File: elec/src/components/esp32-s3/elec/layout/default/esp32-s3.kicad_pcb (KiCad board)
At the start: 2 copper layers, 6 parts

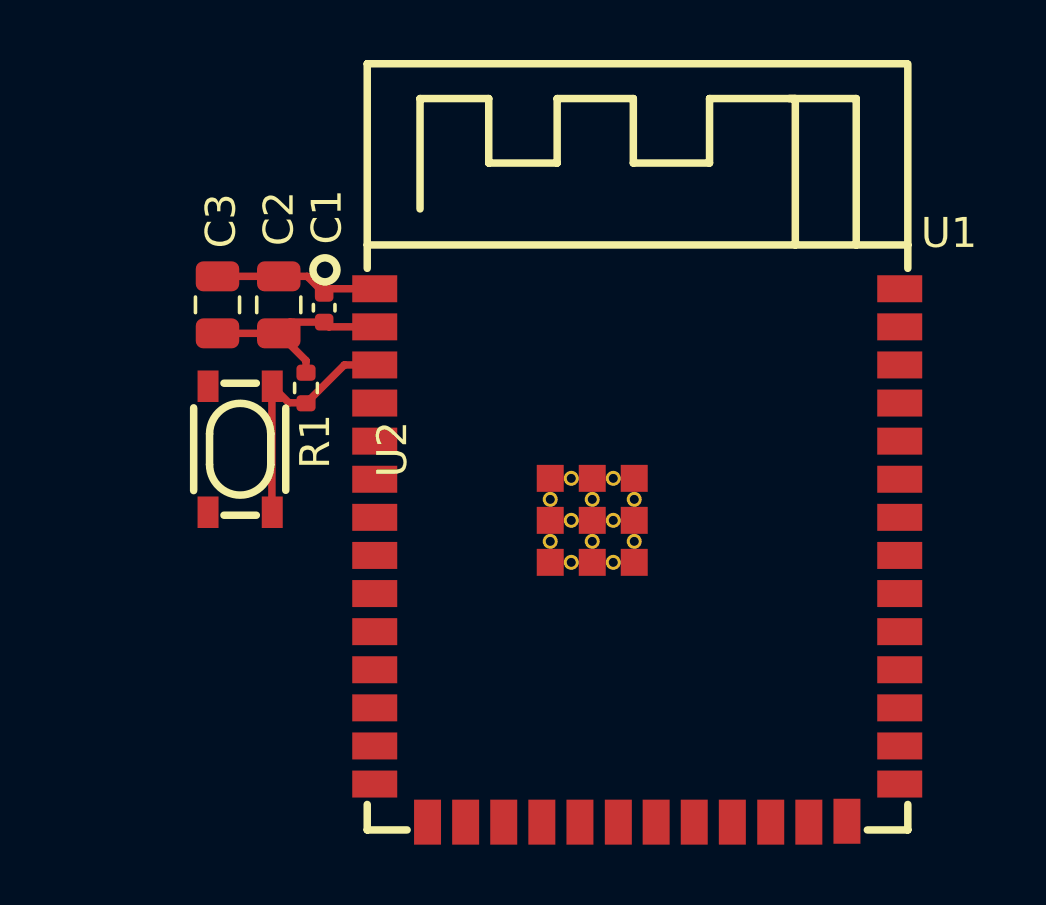
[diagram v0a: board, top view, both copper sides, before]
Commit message: Layout controller block
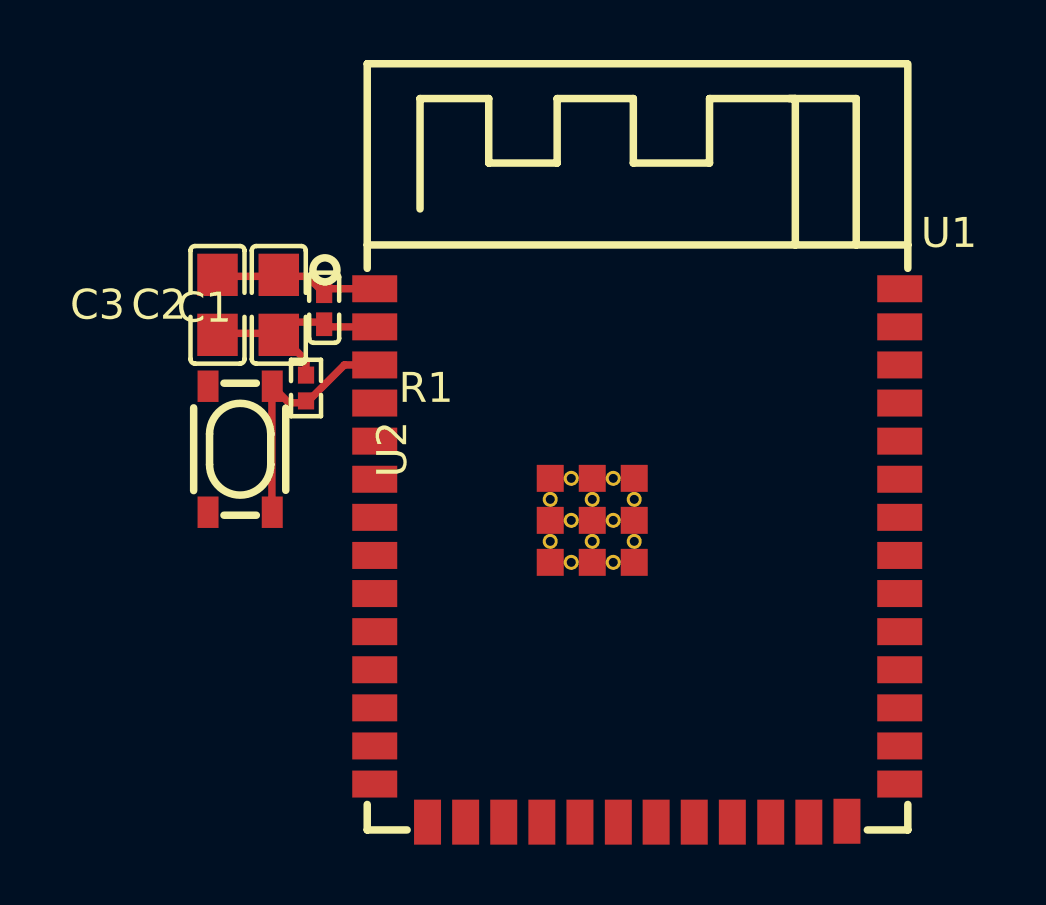
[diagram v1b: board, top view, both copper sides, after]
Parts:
- C1: value 16V 100nF X7R ±10% 0402 Multilayer Ceramic Capacitors MLCC - SMD/SMT ROHS -> 100nF ±10% 16V X7R; footprint lib:C0402 -> atopile:C0402-b3ef17
- C2, C3: value 25V 10uF X5R ±10% 0805 Multilayer Ceramic Capacitors MLCC - SMD/SMT ROHS -> 10µF ±10% 25V X5R; footprint lib:C0805 -> atopile:C0805-3b2e55
- R1: value 62.5mW Thick Film Resistors ±100ppm/℃ ±1% 10kΩ 0402 Chip Resistor - Surface Mount ROHS -> 10kΩ ±1% 62.5mW; footprint lib:R0402 -> atopile:R0402-56259e
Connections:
- net en renamed in
- net ic-gnd renamed gnd
- net io10 renamed cs
- net io11 renamed mosi
- net io12 renamed sck
- net io13 renamed miso
- net io19 renamed dm
- net io20 renamed dp
- net io39 renamed tck
- net io40 renamed tdo
- net io41 renamed tdi
- net io42 renamed tms
- net io6 renamed line
- net io7 renamed line-1
- net rxd0 renamed RXD0
- net txd0 renamed TXD0
- net vcc renamed hv
